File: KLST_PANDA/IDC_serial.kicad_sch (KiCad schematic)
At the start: 2 parts, among them J13 UART

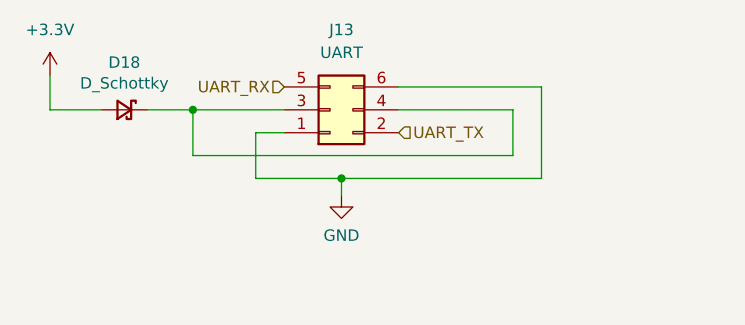
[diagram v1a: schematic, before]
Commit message: started spec'ing components
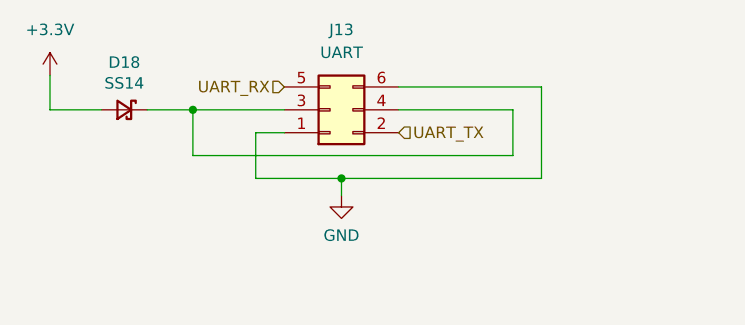
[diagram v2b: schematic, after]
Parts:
- D18: value D_Schottky -> SS14; footprint Diode_SMD:D_SOD-123 -> Diode_SMD:D_SMA; JLCPCB (none) -> C2480; JLCPCB Part # C8598 -> (none)
- J13: JLCPCB (none) -> C146629; JLCPCB Part # C146629 -> (none)
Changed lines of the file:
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@@
       (effects (font (size 1.27 1.27)))
     )
-    (property "Value" "D_Schottky" (at 125.73 98.6536 0)
+    (property "Value" "SS14" (at 125.73 98.6536 0)
       (effects (font (size 1.27 1.27)))
     )
-    (property "Footprint" "Diode_SMD:D_SOD-123" (at 125.73 101.6 90)
+    (property "Footprint" "Diode_SMD:D_SMA" (at 125.73 101.6 90)
       (effects (font (size 1.27 1.27)) hide)
     )
@@
       (effects (font (size 1.27 1.27)) hide)
     )
-    (property "JLCPCB Part #" "C8598" (at 125.73 101.6 0)
+    (property "JLCPCB Part #" "" (at 125.73 101.6 0)
+      (effects (font (size 1.27 1.27)) hide)
+    )
+    (property "JLCPCB" "C2480" (at 125.73 101.6 0)
       (effects (font (size 1.27 1.27)) hide)
     )
@@
       (effects (font (size 1.27 1.27)) hide)
     )
-    (property "JLCPCB Part #" "C146629" (at 148.59 101.6 0)
+    (property "JLCPCB Part #" "" (at 148.59 101.6 0)
       (effects (font (size 1.27 1.27)) hide)
     )
+    (property "JLCPCB" "C146629" (at 148.59 101.6 0)
+      (effects (font (size 1.27 1.27)) hide)
+    )

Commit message: cleaned up footprint assignment
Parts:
- D18: Extended Part - -> (none); MFR.Part # B5819W -> (none)
- J13: Extended Part - -> (none); MFR.Part # 300R-6P -> (none)
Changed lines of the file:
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@@
-      (effects (font (size 1.27 1.27)) hide)
-    )
-    (property "MFR.Part #" "B5819W" (at 125.73 101.6 0)
-      (effects (font (size 1.27 1.27)) hide)
-    )
-    (property "LCSC Part #" "" (at 125.73 101.6 0)
-      (effects (font (size 1.27 1.27)) hide)
-    )
-    (property "Extended Part" "-" (at 125.73 101.6 0)
-      (effects (font (size 1.27 1.27)) hide)
-    )
-    (property "JLCPCB Part #" "" (at 125.73 101.6 0)
       (effects (font (size 1.27 1.27)) hide)
     )
@@
       (effects (font (size 1.27 1.27)) hide)
     )
-    (property "MFR.Part #" "300R-6P" (at 148.59 101.6 0)
-      (effects (font (size 1.27 1.27)) hide)
-    )
-    (property "LCSC Part #" "" (at 148.59 101.6 0)
-      (effects (font (size 1.27 1.27)) hide)
-    )
-    (property "Extended Part" "-" (at 148.59 101.6 0)
-      (effects (font (size 1.27 1.27)) hide)
-    )
-    (property "JLCPCB Part #" "" (at 148.59 101.6 0)
-      (effects (font (size 1.27 1.27)) hide)
-    )

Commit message: distributed modules
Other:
- note added: "@TODO(maybe replace THT with SMD connector e.g C720733 )"
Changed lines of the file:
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@@
     (stroke (width 0) (type default))
+  )
+  (text "@TODO(maybe replace THT with SMD connector e.g C720733 )"
+    (at 121.92 123.19 0)
+    (effects (font (size 1.27 1.27)) (justify left bottom))
   )
   (hierarchical_label "UART_TX" (shape input) (at 156.21 104.14 0) (fields_autoplaced)
